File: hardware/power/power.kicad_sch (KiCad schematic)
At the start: 18 parts, among them J1 Screw_Terminal_01x02, J2 Screw_Terminal_01x03, Q1 BSS123, U1 AL8861

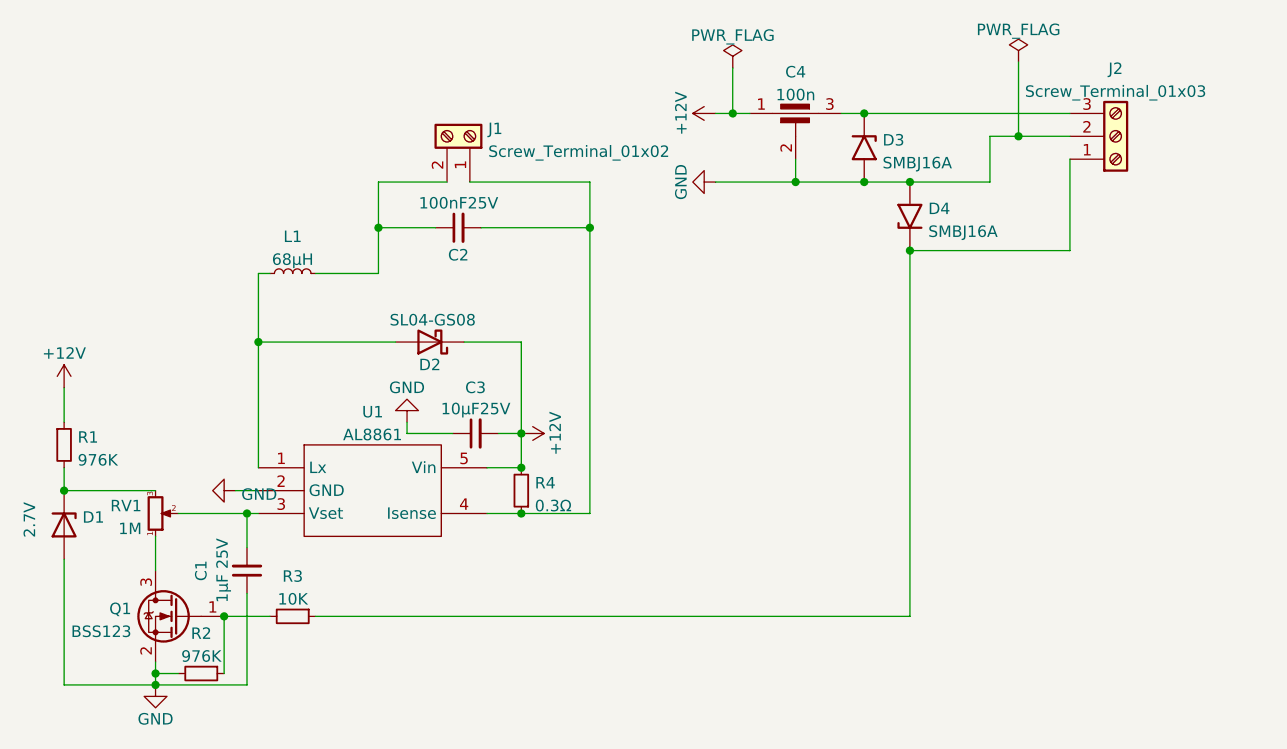
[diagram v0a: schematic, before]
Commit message: change connectors for SMD ones
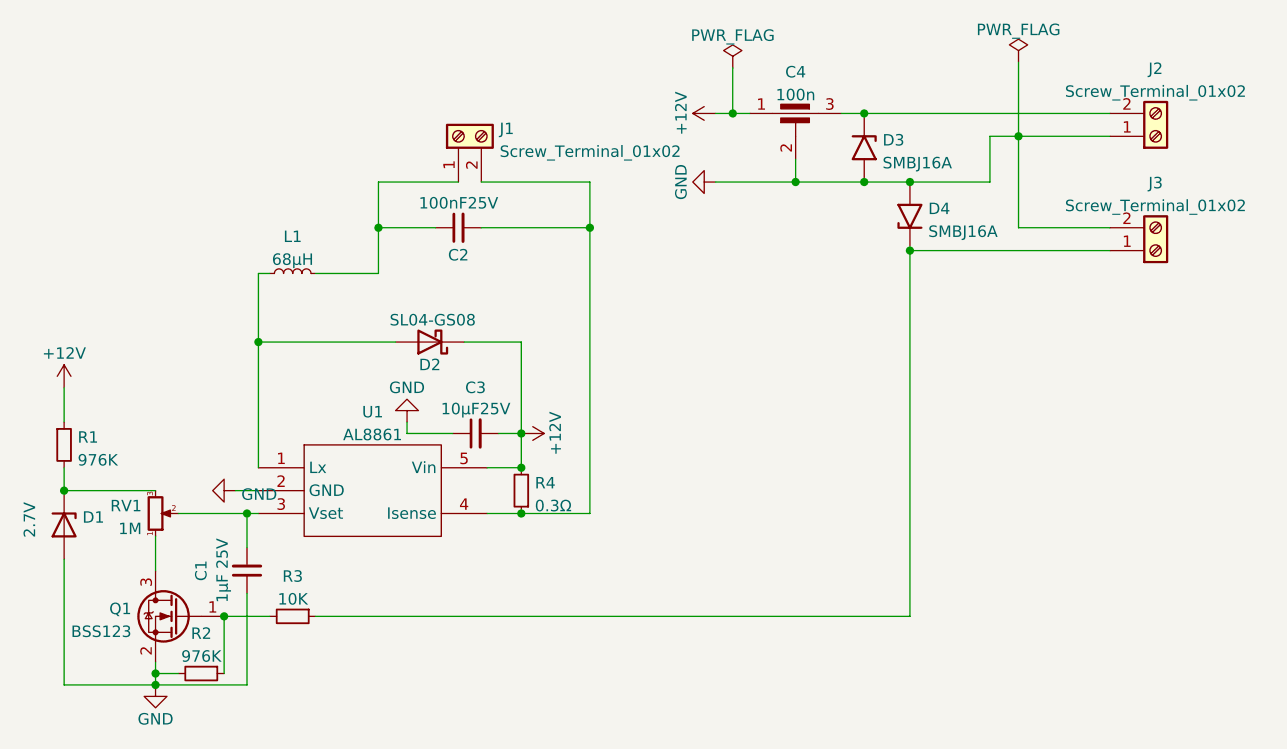
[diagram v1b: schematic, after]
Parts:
- removed J2: Screw_Terminal_01x03, TerminalBlock_TE-Connectivity:TerminalBlock_TE_282834-3_1x03_P2.54mm_Horizontal, symbol Connector:Screw_Terminal_01x03
- added J2, J3: Screw_Terminal_01x02, local:amphenol_TZ02, symbol Connector:Screw_Terminal_01x02
- J1: footprint TerminalBlock_TE-Connectivity:TerminalBlock_TE_282834-2_1x02_P2.54mm_Horizontal -> local:amphenol_TZ02; P/N (none) -> TZ022101B000G
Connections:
- net GND: now also J2.1 (Pin_1), J3.2 (Pin_2)
- net at C2.2, R4.1, U1.4 (Isense): now also J1.2 (Pin_2); no longer J1.1 (Pin_1)
- net at C2.1, L1.2: now also J1.1 (Pin_1); no longer J1.2 (Pin_2)
- net at C4.3, D3.1 (A1): now also J2.2 (Pin_2)
- net at D4.1 (A1), R3.1: now also J3.1 (Pin_1)
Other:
- moved on the sheet: J1
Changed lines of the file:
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@@
+    (stroke (width 0) (type default) (color 0 0 0 0))
+  )
+  (wire (pts (xy 206.375 67.31) (xy 206.375 57.15))
     (stroke (width 0) (type default) (color 0 0 0 0))
   )
@@
     (stroke (width 0) (type default) (color 0 0 0 0))
   )
+  (wire (pts (xy 216.535 67.31) (xy 206.375 67.31))
+    (stroke (width 0) (type default) (color 0 0 0 0))
+  )
   (wire (pts (xy 121.92 80.01) (xy 137.16 80.01))
     (stroke (width 0) (type default) (color 0 0 0 0))
   )
-  (wire (pts (xy 206.375 57.15) (xy 212.09 57.15))
+  (wire (pts (xy 206.375 57.15) (xy 216.535 57.15))
     (stroke (width 0) (type default) (color 0 0 0 0))
   )
@@
     (stroke (width 0) (type default) (color 0 0 0 0))
   )
-  (wire (pts (xy 194.31 69.85) (xy 212.09 69.85))
+  (wire (pts (xy 194.31 69.85) (xy 216.535 69.85))
     (stroke (width 0) (type default) (color 0 0 0 0))
   )
@@
     (stroke (width 0) (type default) (color 0 0 0 0))
   )
-  (wire (pts (xy 189.23 54.61) (xy 212.09 54.61))
-    (stroke (width 0) (type default) (color 0 0 0 0))
-  )
   (wire (pts (xy 135.255 62.23) (xy 135.255 67.31))
     (stroke (width 0) (type default) (color 0 0 0 0))
@@
     (stroke (width 0) (type default) (color 0 0 0 0))
   )
+  (wire (pts (xy 146.685 62.23) (xy 158.75 62.23))
+    (stroke (width 0) (type default) (color 0 0 0 0))
+  )
   (wire (pts (xy 174.625 54.61) (xy 176.53 54.61))
     (stroke (width 0) (type default) (color 0 0 0 0))
@@
     (stroke (width 0) (type default) (color 0 0 0 0))
   )
+  (wire (pts (xy 189.23 54.61) (xy 216.535 54.61))
+    (stroke (width 0) (type default) (color 0 0 0 0))
+  )
   (wire (pts (xy 151.13 80.01) (xy 144.78 80.01))
     (stroke (width 0) (type default) (color 0 0 0 0))
   )
-  (wire (pts (xy 212.09 69.85) (xy 212.09 59.69))
-    (stroke (width 0) (type default) (color 0 0 0 0))
-  )
   (wire (pts (xy 121.92 72.39) (xy 121.92 80.01))
     (stroke (width 0) (type default) (color 0 0 0 0))
@@
     (stroke (width 0) (type default) (color 0 0 0 0))
   )
-  (wire (pts (xy 145.415 62.23) (xy 158.75 62.23))
-    (stroke (width 0) (type default) (color 0 0 0 0))
-  )
   (wire (pts (xy 186.69 54.61) (xy 189.23 54.61))
     (stroke (width 0) (type default) (color 0 0 0 0))
@@
     (stroke (width 0) (type default) (color 0 0 0 0))
   )
-  (wire (pts (xy 142.875 62.23) (xy 135.255 62.23))
+  (wire (pts (xy 135.255 62.23) (xy 144.145 62.23))
     (stroke (width 0) (type default) (color 0 0 0 0))
   )
@@
     (pin "2")
   )
+  (symbol (lib_id "Connector:Screw_Terminal_01x02") (at 221.615 69.85 0) (mirror x) (unit 1)
+    (in_bom yes) (on_board yes) (fields_autoplaced)
+    (property "Reference" "J3" (id 0) (at 221.615 62.3402 0))
+    (property "Value" "Screw_Terminal_01x02" (id 1) (at 221.615 64.8771 0))
+    (property "Footprint" "local:amphenol_TZ02" (id 2) (at 221.615 69.85 0)
+      (effects (font (size 1.27 1.27)) hide)
+    )
+    (property "Datasheet" "~" (id 3) (at 221.615 69.85 0)
+      (effects (font (size 1.27 1.27)) hide)
+    )
+    (property "P/N" "TZ022101B000G " (id 4) (at 221.615 69.85 90)
+      (effects (font (size 1.27 1.27)) hide)
+    )
+    (pin "1")
+    (pin "2")
+  )
   (symbol (lib_id "power:GND") (at 138.43 88.9 180) (unit 1)
     (in_bom yes) (on_board yes)
@@
     (pin "2")
   )
+  (symbol (lib_id "Connector:Screw_Terminal_01x02") (at 221.615 57.15 0) (mirror x) (unit 1)
+    (in_bom yes) (on_board yes) (fields_autoplaced)
+    (property "Reference" "J2" (id 0) (at 221.615 49.6402 0))
+    (property "Value" "Screw_Terminal_01x02" (id 1) (at 221.615 52.1771 0))
+    (property "Footprint" "local:amphenol_TZ02" (id 2) (at 221.615 57.15 0)
+      (effects (font (size 1.27 1.27)) hide)
+    )
+    (property "Datasheet" "~" (id 3) (at 221.615 57.15 0)
+      (effects (font (size 1.27 1.27)) hide)
+    )
+    (property "P/N" "TZ022101B000G " (id 4) (at 221.615 57.15 90)
+      (effects (font (size 1.27 1.27)) hide)
+    )
+    (pin "1")
+    (pin "2")
+  )
   (symbol (lib_id "Device:Q_NMOS_GSD") (at 113.03 110.49 0) (mirror y) (unit 1)
     (in_bom yes) (on_board yes) (fields_autoplaced)
@@
     (pin "2")
   )
-  (symbol (lib_id "Connector:Screw_Terminal_01x03") (at 217.17 57.15 0) (mirror x) (unit 1)
-    (in_bom yes) (on_board yes) (fields_autoplaced)
-    (property "Reference" "J2" (id 0) (at 217.17 49.6402 0))
-    (property "Value" "Screw_Terminal_01x03" (id 1) (at 217.17 52.1771 0))
-    (property "Footprint" "TerminalBlock_TE-Connectivity:TerminalBlock_TE_282834-3_1x03_P2.54mm_Horizontal" (id 2) (at 217.17 57.15 0)
-      (effects (font (size 1.27 1.27)) hide)
-    )
-    (property "Datasheet" "~" (id 3) (at 217.17 57.15 0)
-      (effects (font (size 1.27 1.27)) hide)
-    )
-    (property "P/N" "282834-3 (stock)" (id 4) (at 217.17 57.15 0)
-      (effects (font (size 1.27 1.27)) hide)
-    )
-    (pin "1")
-    (pin "2")
-    (pin "3")
-  )
-  (symbol (lib_id "Connector:Screw_Terminal_01x02") (at 145.415 57.15 270) (mirror x) (unit 1)
-    (in_bom yes) (on_board yes) (fields_autoplaced)
-    (property "Reference" "J1" (id 0) (at 147.447 56.3153 90)
-      (effects (font (size 1.27 1.27)) (justify left))
-    )
-    (property "Value" "Screw_Terminal_01x02" (id 1) (at 147.447 58.8522 90)
-      (effects (font (size 1.27 1.27)) (justify left))
-    )
-    (property "Footprint" "TerminalBlock_TE-Connectivity:TerminalBlock_TE_282834-2_1x02_P2.54mm_Horizontal" (id 2) (at 145.415 57.15 0)
-      (effects (font (size 1.27 1.27)) hide)
-    )
-    (property "Datasheet" "~" (id 3) (at 145.415 57.15 0)
+  (symbol (lib_id "Connector:Screw_Terminal_01x02") (at 144.145 57.15 90) (unit 1)
+    (in_bom yes) (on_board yes) (fields_autoplaced)
+    (property "Reference" "J1" (id 0) (at 148.717 56.3153 90)
+      (effects (font (size 1.27 1.27)) (justify right))
+    )
+    (property "Value" "Screw_Terminal_01x02" (id 1) (at 148.717 58.8522 90)
+      (effects (font (size 1.27 1.27)) (justify right))
+    )
+    (property "Footprint" "local:amphenol_TZ02" (id 2) (at 144.145 57.15 0)
+      (effects (font (size 1.27 1.27)) hide)
+    )
+    (property "Datasheet" "~" (id 3) (at 144.145 57.15 0)
+      (effects (font (size 1.27 1.27)) hide)
+    )
+    (property "P/N" "TZ022101B000G " (id 4) (at 144.145 57.15 90)
       (effects (font (size 1.27 1.27)) hide)
     )
@@
     )
     (path "/c442a30e-7a87-4e31-a0bd-0378c325bac4"
-      (reference "J1") (unit 1) (value "Screw_Terminal_01x02") (footprint "TerminalBlock_TE-Connectivity:TerminalBlock_TE_282834-2_1x02_P2.54mm_Horizontal")
-    )
-    (path "/bf06e978-418f-42d7-bbde-c8a97f9d162c"
-      (reference "J2") (unit 1) (value "Screw_Terminal_01x03") (footprint "TerminalBlock_TE-Connectivity:TerminalBlock_TE_282834-3_1x03_P2.54mm_Horizontal")
+      (reference "J1") (unit 1) (value "Screw_Terminal_01x02") (footprint "local:amphenol_TZ02")
+    )
+    (path "/a092ec95-e9c3-4eac-a52a-f524f44fb4e1"
+      (reference "J2") (unit 1) (value "Screw_Terminal_01x02") (footprint "local:amphenol_TZ02")
+    )
+    (path "/4638e3a4-9e98-42cf-99ca-190bde8fc639"
+      (reference "J3") (unit 1) (value "Screw_Terminal_01x02") (footprint "local:amphenol_TZ02")
     )
     (path "/52194c94-e7df-49ff-beb1-04a1b4f2344e"
